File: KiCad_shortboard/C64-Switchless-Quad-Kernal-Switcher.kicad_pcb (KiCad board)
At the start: 2 copper layers, 22.2 x 46.4 mm, 10 parts, among them J1 01x14_precision_pinlist, J2 01x14_precision_pinlist, J3 27C256/512_28PDIP, J4 Wireconnections, U1 ATtiny85-20PU, U2 74LS08

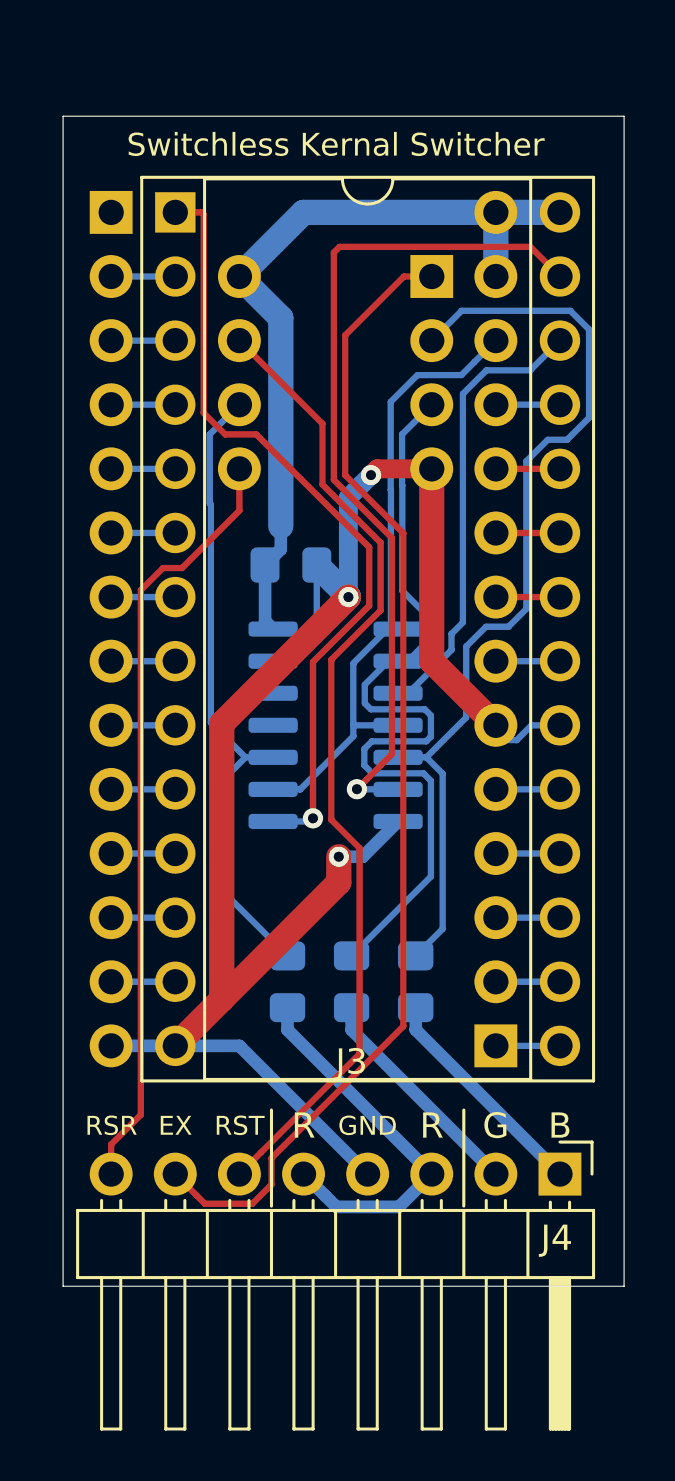
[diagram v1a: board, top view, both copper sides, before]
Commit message: 1541C support in firmware and SKS64 shortboard pcb version
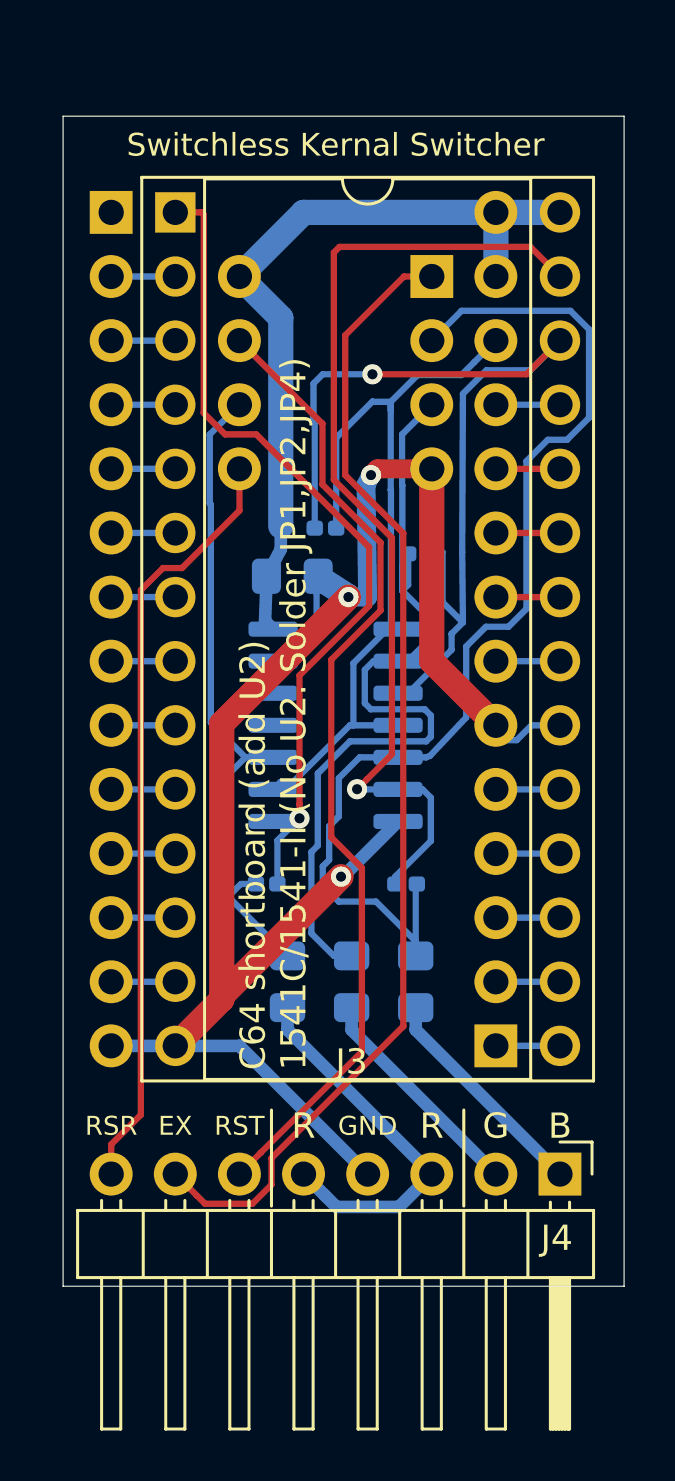
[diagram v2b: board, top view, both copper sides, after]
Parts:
- added JP1: SolderJumper_2_Open, pkl_jumpers:J_0402, B.Cu at (110.3, 85.0)
- added JP2: SolderJumper_2_Open, pkl_jumpers:J_0402, B.Cu at (115.8, 85.0)
- added JP3: SolderJumper_2_Open, pkl_jumpers:J_0402, B.Cu at (116.3, 71.9)
- added JP4: SolderJumper_2_Open, pkl_jumpers:J_0402, B.Cu at (112.6, 70.9)
- moved C1 0.45 mm to (111.3, 72.8)
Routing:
- net /A13: track 17.9 -> 37.8 mm, vias 0 -> 1
- net /MCU_A14: track 37.3 -> 44.0 mm
- net /~BASIC~_KERNAL: track 25.2 -> 31.7 mm
- net /A14: track 34.0 -> 39.4 mm
- net /A15: track 31.1 -> 33.8 mm
- net /MCU_A13: track 32.6 -> 34.4 mm
- net /MCU_A15: track 25.3 -> 26.6 mm
- net GND: track 73.5 -> 72.7 mm
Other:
- board text added: "BWACK 2021"
- board text added: "C64 shortboard (add U2) 1541C/1541-II (No U2. Solder JP1,JP2,JP4)"
- board text added: "C64 shortboard V1.1"
- board text removed: "BWACK 2019"
- board text removed: "C64 shortboard V1.0"
